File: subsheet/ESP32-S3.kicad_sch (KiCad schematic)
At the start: 14 parts, among them J201 Conn_01x06, SW201 SW_Push, SW202 SW_Push, U201 TLV75533PDBV, U202 ESP32-S3-MINI-1

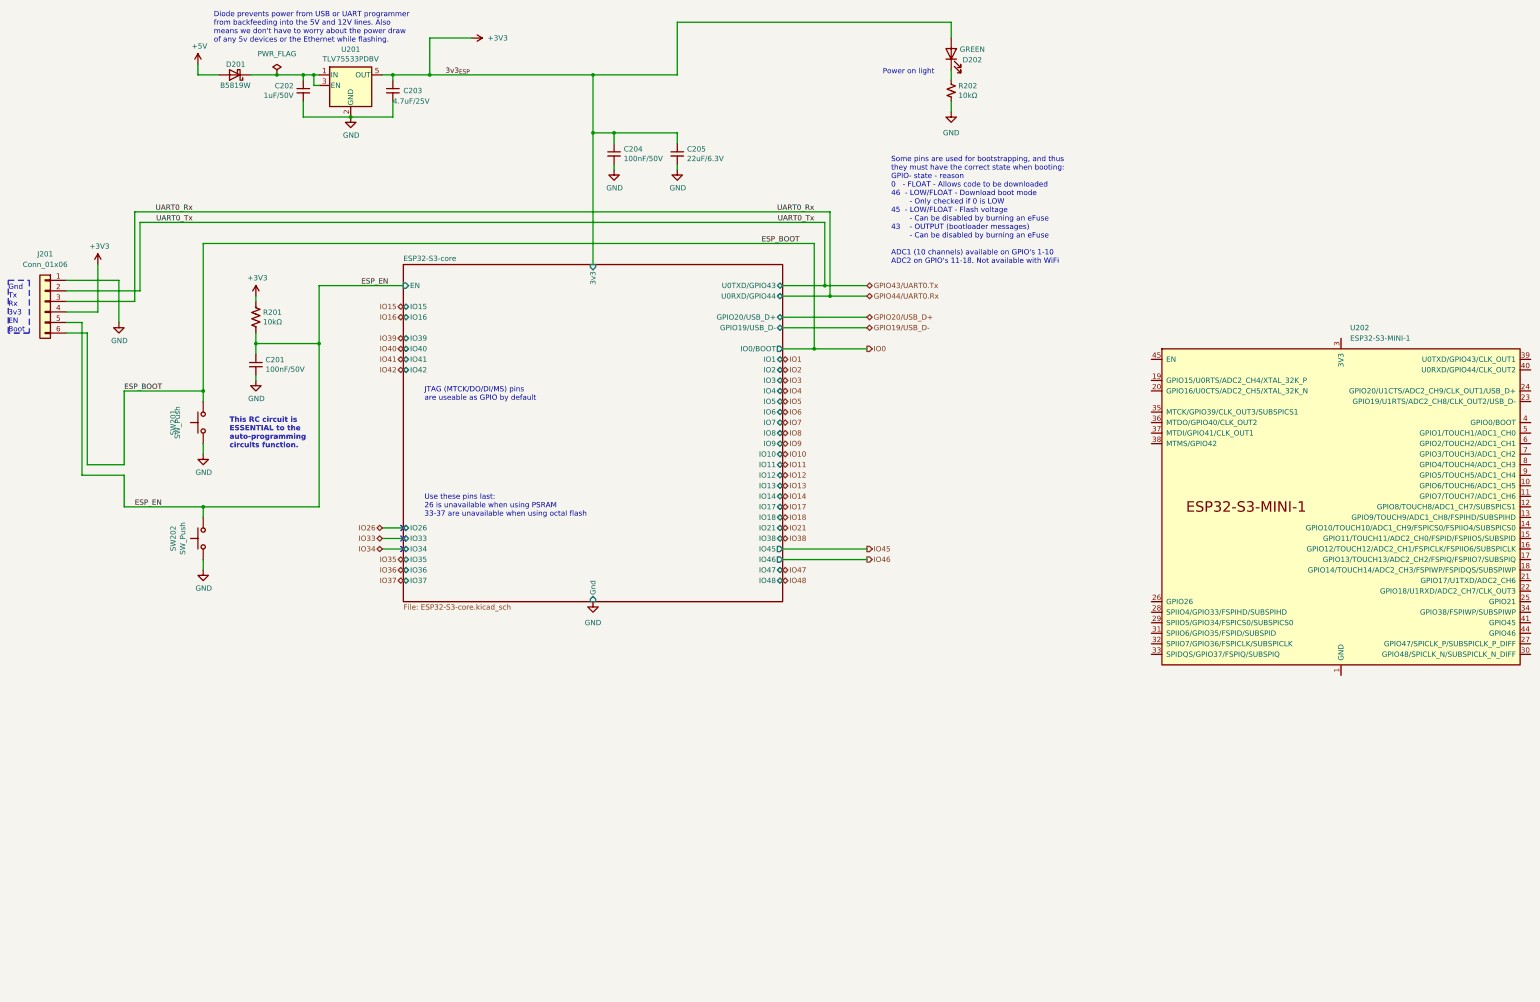
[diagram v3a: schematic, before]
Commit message: PCB changes, added useful connectors
Added a whole bunch of things that should make it useful - e.g.
ethernet, an extra flash chip for general storage, piicodev connectors
for I2C.

Also added a GPIB connector footprint; dev-board version worked nicely,
but may as well make this work for that too. Saves bying dev boards : )
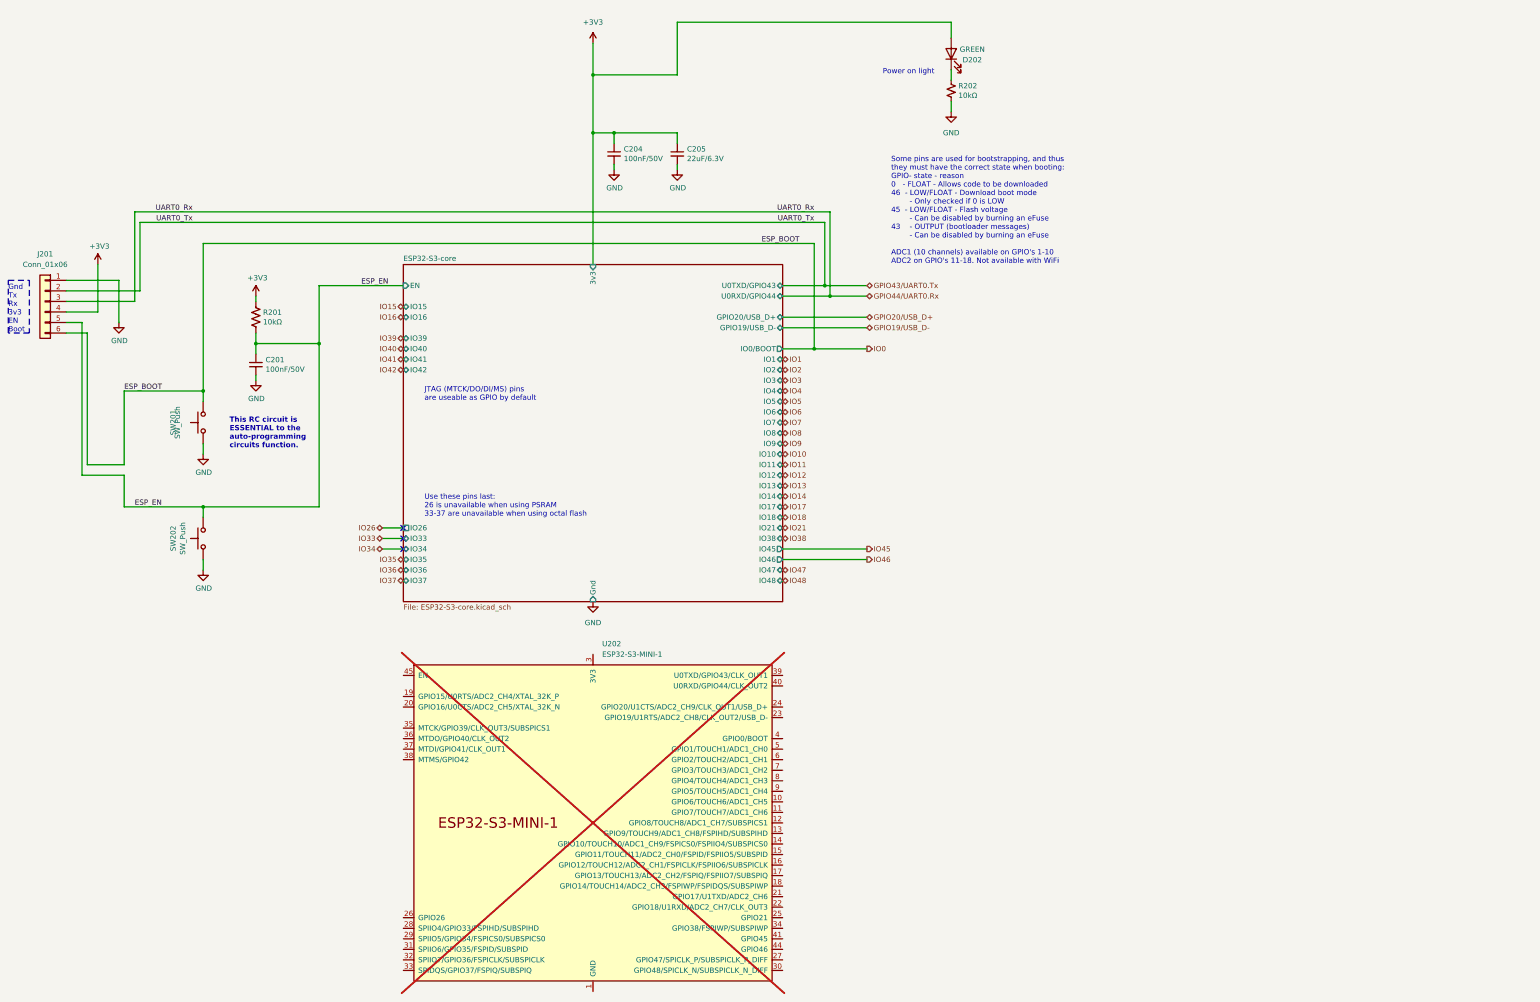
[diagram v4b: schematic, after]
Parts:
- removed C202: 1uF/50V, Capacitor_SMD:C_0805_2012Metric, symbol Device:C_Small
- removed C203: 4.7uF/25V, Capacitor_SMD:C_0805_2012Metric, symbol Device:C_Small
- removed D201: B5819W, Diode_SMD:D_SOD-123, symbol Device:D_Schottky
- removed U201: TLV75533PDBV, Package_TO_SOT_SMD:SOT-23-5, symbol Regulator_Linear:TLV75533PDBV
- U202: now not fitted; now left out of the parts list
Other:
- note removed: "Diode prevents power from USB or UART programmer from backfeeding into the 5V and 12V lines. Also means we don't have to worry about the power draw of any 5v devices or the Ethernet while flashing."

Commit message: Uknown changes?File formats?
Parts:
- renumbered C204 to C202, C205 to C203, D202 to D201, U202 to U201
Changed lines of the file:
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@@
 		(on_board yes)
 		(dnp no)
-		(property "Reference" "#PWR0204"
+		(property "Reference" "#PWR0203"
 			(at 63.5 125.73 0)
 			(effects
@@
 			(project "ESP_bare_chip_test_board"
 				(path "/45b6f84a-e69b-48be-a49b-bc68872e2c15/20c7e844-38a5-4683-b2ad-60f2017be075"
-					(reference "#PWR0204")
+					(reference "#PWR0203")
 					(unit 1)
 				)
@@
 		(on_board yes)
 		(dnp no)
-		(property "Reference" "#PWR0211"
+		(property "Reference" "#PWR0209"
 			(at 162.56 57.15 0)
 			(effects
@@
 			(project "ESP_bare_chip_test_board"
 				(path "/45b6f84a-e69b-48be-a49b-bc68872e2c15/20c7e844-38a5-4683-b2ad-60f2017be075"
-					(reference "#PWR0211")
+					(reference "#PWR0209")
 					(unit 1)
 				)
@@
 		(on_board yes)
 		(dnp no)
-		(property "Reference" "D202"
+		(property "Reference" "D201"
 			(at 248.92 24.3205 90)
 			(effects
@@
 			(project "ESP_bare_chip_test_board"
 				(path "/45b6f84a-e69b-48be-a49b-bc68872e2c15/20c7e844-38a5-4683-b2ad-60f2017be075"
-					(reference "D202")
+					(reference "D201")
 					(unit 1)
 				)
@@
 		(on_board yes)
 		(dnp no)
-		(property "Reference" "#PWR0205"
+		(property "Reference" "#PWR0204"
 			(at 63.5 153.67 0)
 			(effects
@@
 			(project "ESP_bare_chip_test_board"
 				(path "/45b6f84a-e69b-48be-a49b-bc68872e2c15/20c7e844-38a5-4683-b2ad-60f2017be075"
-					(reference "#PWR0205")
+					(reference "#PWR0204")
 					(unit 1)
 				)
@@
 		(dnp yes)
 		(fields_autoplaced yes)
-		(property "Reference" "U202"
+		(property "Reference" "U201"
 			(at 159.6741 165.1 0)
 			(effects
@@
 			(project "ESP_bare_chip_test_board"
 				(path "/45b6f84a-e69b-48be-a49b-bc68872e2c15/20c7e844-38a5-4683-b2ad-60f2017be075"
-					(reference "U202")
+					(reference "U201")
 					(unit 1)
 				)
@@
 		(dnp no)
 		(fields_autoplaced yes)
-		(property "Reference" "#PWR0214"
+		(property "Reference" "#PWR0207"
 			(at 157.48 24.13 0)
 			(effects
@@
 			(project "ESP_bare_chip_test_board"
 				(path "/45b6f84a-e69b-48be-a49b-bc68872e2c15/20c7e844-38a5-4683-b2ad-60f2017be075"
-					(reference "#PWR0214")
+					(reference "#PWR0207")
 					(unit 1)
 				)
@@
 		(on_board yes)
 		(dnp no)
-		(property "Reference" "C205"
+		(property "Reference" "C203"
 			(at 180.1368 45.8216 0)
 			(effects
@@
 			(project "ESP_bare_chip_test_board"
 				(path "/45b6f84a-e69b-48be-a49b-bc68872e2c15/20c7e844-38a5-4683-b2ad-60f2017be075"
-					(reference "C205")
+					(reference "C203")
 					(unit 1)
 				)
@@
 		(on_board yes)
 		(dnp no)
-		(property "Reference" "#PWR0212"
+		(property "Reference" "#PWR0210"
 			(at 177.8 57.15 0)
 			(effects
@@
 			(project "ESP_bare_chip_test_board"
 				(path "/45b6f84a-e69b-48be-a49b-bc68872e2c15/20c7e844-38a5-4683-b2ad-60f2017be075"
-					(reference "#PWR0212")
+					(reference "#PWR0210")
 					(unit 1)
 				)
@@
 		(on_board yes)
 		(dnp no)
-		(property "Reference" "#PWR0207"
+		(property "Reference" "#PWR0206"
 			(at 76.2 107.95 0)
 			(effects
@@
 			(project "ESP_bare_chip_test_board"
 				(path "/45b6f84a-e69b-48be-a49b-bc68872e2c15/20c7e844-38a5-4683-b2ad-60f2017be075"
-					(reference "#PWR0207")
+					(reference "#PWR0206")
 					(unit 1)
 				)
@@
 		(on_board yes)
 		(dnp no)
-		(property "Reference" "C204"
+		(property "Reference" "C202"
 			(at 164.8968 45.8216 0)
 			(effects
@@
 			(project "ESP_bare_chip_test_board"
 				(path "/45b6f84a-e69b-48be-a49b-bc68872e2c15/20c7e844-38a5-4683-b2ad-60f2017be075"
-					(reference "C204")
+					(reference "C202")
 					(unit 1)
 				)
@@
 		(on_board yes)
 		(dnp no)
-		(property "Reference" "#PWR0206"
+		(property "Reference" "#PWR0205"
 			(at 76.2 85.09 0)
 			(effects
@@
 			(project "ESP_bare_chip_test_board"
 				(path "/45b6f84a-e69b-48be-a49b-bc68872e2c15/20c7e844-38a5-4683-b2ad-60f2017be075"
-					(reference "#PWR0206")
+					(reference "#PWR0205")
 					(unit 1)
 				)
@@
 		(dnp no)
 		(fields_autoplaced yes)
-		(property "Reference" "#PWR0210"
+		(property "Reference" "#PWR0208"
 			(at 157.48 161.29 0)
 			(effects
@@
 			(project "ESP_bare_chip_test_board"
 				(path "/45b6f84a-e69b-48be-a49b-bc68872e2c15/20c7e844-38a5-4683-b2ad-60f2017be075"
-					(reference "#PWR0210")
+					(reference "#PWR0208")
 					(unit 1)
 				)
@@
 		(dnp no)
 		(fields_autoplaced yes)
-		(property "Reference" "#PWR0213"
+		(property "Reference" "#PWR0211"
 			(at 243.84 43.18 0)
 			(effects
@@
 			(project "ESP_bare_chip_test_board"
 				(path "/45b6f84a-e69b-48be-a49b-bc68872e2c15/20c7e844-38a5-4683-b2ad-60f2017be075"
-					(reference "#PWR0213")
-					(unit 1)
-				)
+					(reference "#PWR0211")
+					(unit 1)
+				)

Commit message: Picked part numbers and placed most remaining MCU support components
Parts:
- C202: now not fitted; now left out of the parts list
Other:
- note added: "Small capacitor redundant, lots of them internally"
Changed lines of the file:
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@@
+		)
+	)
+	(text "Small capacitor redundant,\nlots of them internally"
+		(exclude_from_sim no)
+		(at 162.56 40.64 0)
+		(effects
+			(font
+				(size 1.27 1.27)
+			)
+			(justify left bottom)
 		)
 	)
@@
 		(at 162.56 46.99 0)
 		(unit 1)
-		(exclude_from_sim no)
-		(in_bom yes)
-		(on_board yes)
-		(dnp no)
+		(exclude_from_sim yes)
+		(in_bom no)
+		(on_board no)
+		(dnp yes)
 		(property "Reference" "C202"
 			(at 164.8968 45.8216 0)

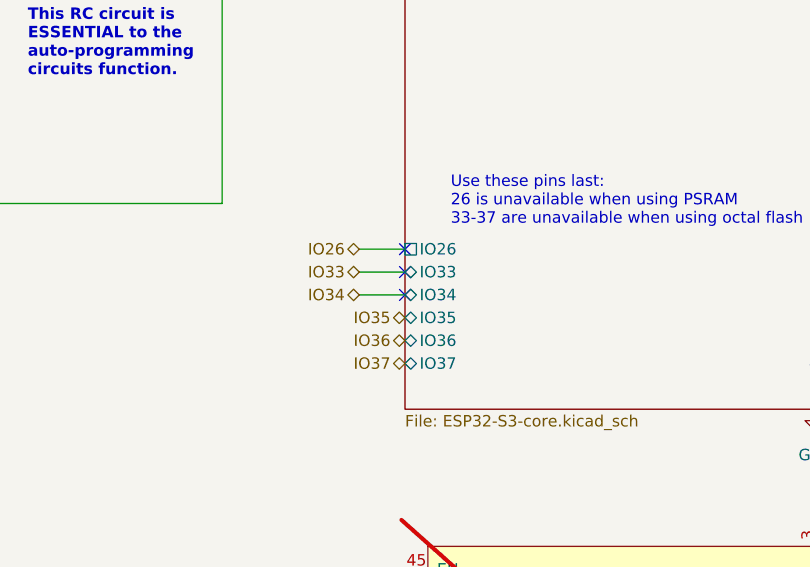
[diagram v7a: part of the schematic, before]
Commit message: More wiring - GPIB connector, partially routed
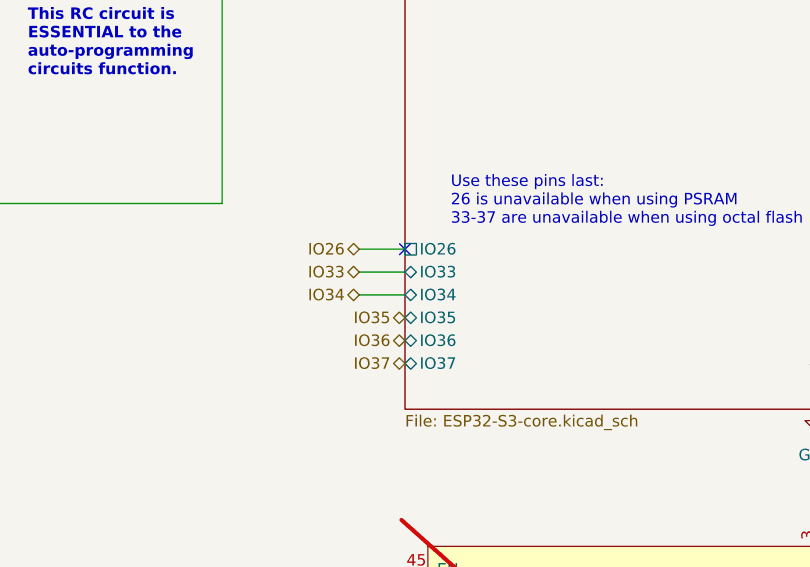
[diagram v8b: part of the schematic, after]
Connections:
- no-connect marks 3 -> 1
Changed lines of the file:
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@@
-	)
-	(no_connect
-		(at 111.76 139.7)
-	)
-	(no_connect
-		(at 111.76 142.24)
 	)
 	(no_connect
